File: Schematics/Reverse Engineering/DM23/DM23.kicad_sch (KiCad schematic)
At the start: 100 parts, among them J1 Conn_01x40, Q1 2N1499A, Q2 2N1499A, Q3 2N1499A, Q4 2N1499A, Q5 2N1499A, Q6 2N1499A, Q7 2N1499A, Q8 2N1499A, Q9 2N1499A

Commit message: Updated Schematic Layout and PCB
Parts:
- R39: footprint (none) -> Resistor_THT:R_Axial_DIN0207_L6.3mm_D2.5mm_P10.16mm_Horizontal
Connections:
- net P11 is gone; now on net J1-11: C20.1
- net P13 is gone; now on net J1-13: D12.2 (A)
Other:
- note added: "C4, C12, C19 - Nytronics Type 105 Polyester Film Cap All Diodes are Germanium All Transistor are 2N1499A All Resistors are 1/2W 5% Carbon Composition"
- note added: "| IN | OUT | | 0V | -12V | |-12V| 0V |"
- note removed: "C4, C12, C19 - Nytronics Type 105 Polyester Filt Cap All Diodes are Germanium All Transistor are 2N1499A All Resistors are 1/2W 5% Carbon Composition"
- note removed: "Check Black Resistor for actual value and tolerance"
- moved on the sheet: C1, C10, C11, C12, C13, C14, C15, C16, C17, C18, C19, C2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

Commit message: LR312 Schematic and PCB
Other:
- note added: "C4, C12, C19 - Nytronics Type 105 Polyester Film Cap All Diodes are Germanium All Transistor are 2N1499A All Resistors are 1/2W 5% Carbon Composition Connector Elco Varicon 7000 or 5203 Series Contacts"
- note removed: "C4, C12, C19 - Nytronics Type 105 Polyester Film Cap All Diodes are Germanium All Transistor are 2N1499A All Resistors are 1/2W 5% Carbon Composition"
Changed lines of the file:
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@@
 		)
 	)
-	(text "C4, C12, C19 - Nytronics Type 105 Polyester Film Cap\nAll Diodes are Germanium\nAll Transistor are 2N1499A\nAll Resistors are 1/2W 5% Carbon Composition "
+	(text "C4, C12, C19 - Nytronics Type 105 Polyester Film Cap\nAll Diodes are Germanium\nAll Transistor are 2N1499A\nAll Resistors are 1/2W 5% Carbon Composition \nConnector Elco Varicon 7000 or 5203 Series Contacts"
 		(exclude_from_sim no)
 		(at 211.836 173.736 0)

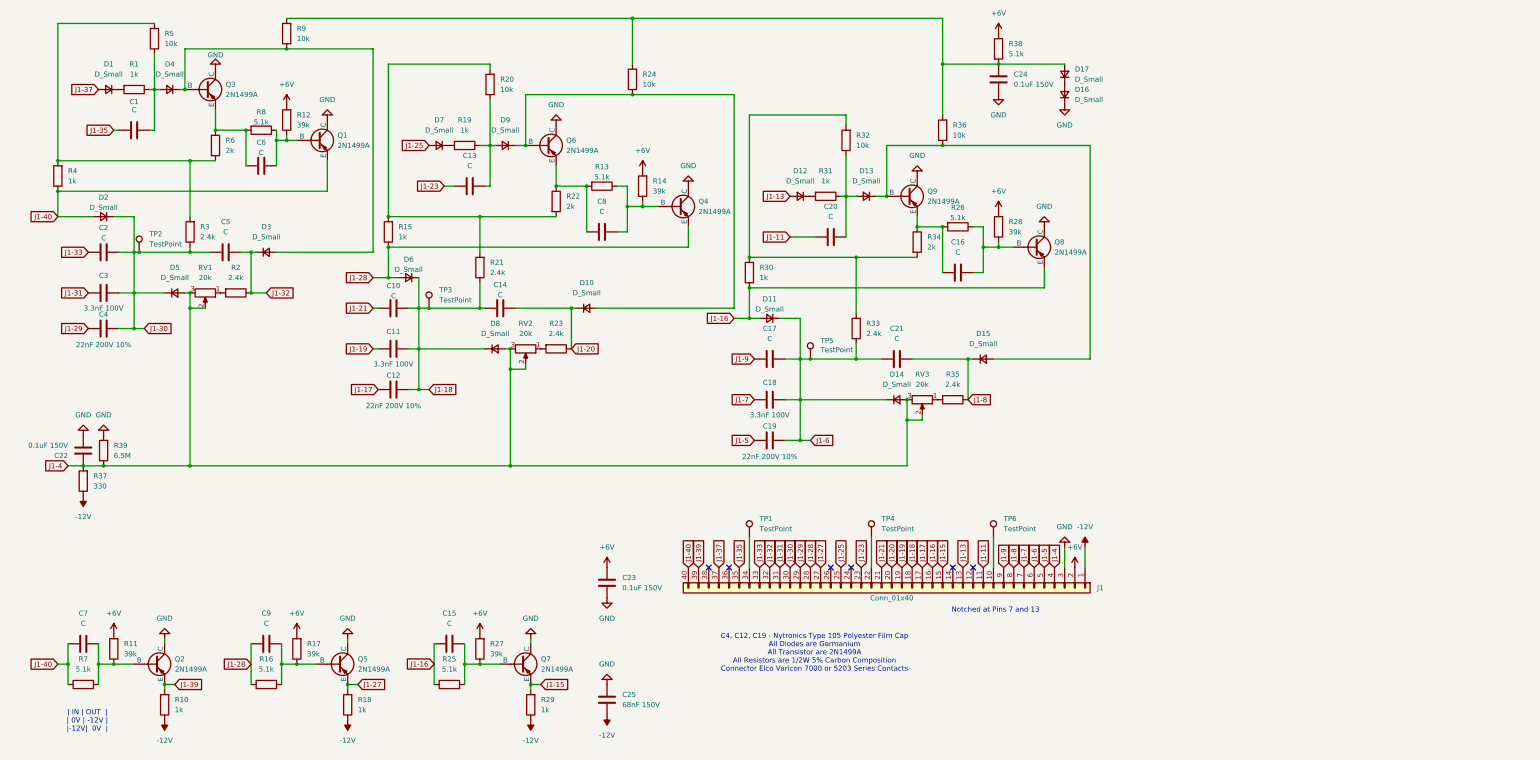
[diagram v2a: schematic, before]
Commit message: DM23 Reverse Engineering Complete
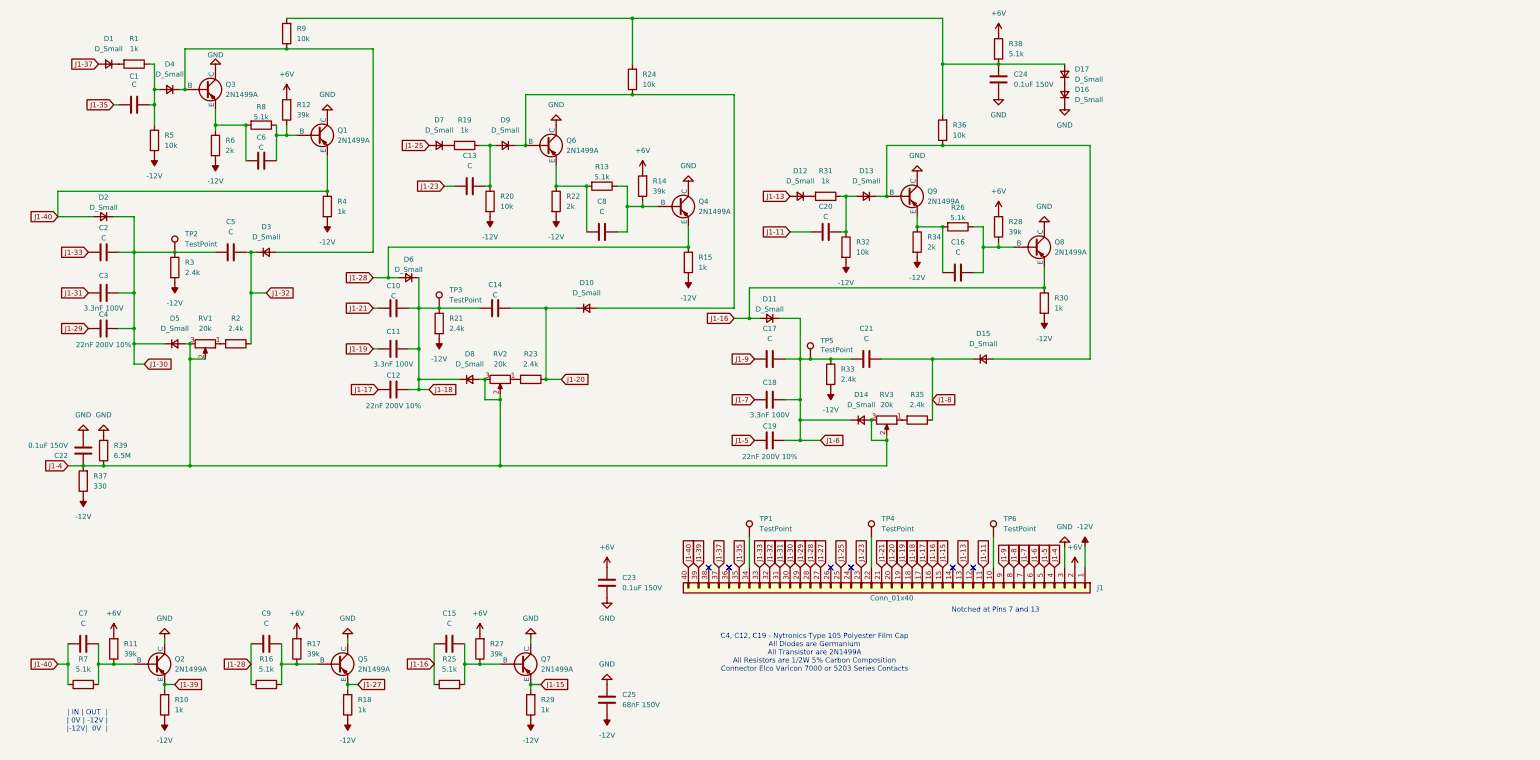
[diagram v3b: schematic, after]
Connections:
- net -12V: now also R15.2, R20.2, R21.2, R22.2, R3.2, R30.2, R32.2, R33.2, R34.2, R4.2, R5.2, R6.2
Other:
- moved on the sheet: C1, C14, C20, C21, C5, C6, D1, D14, D5, D8, Q1, R1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

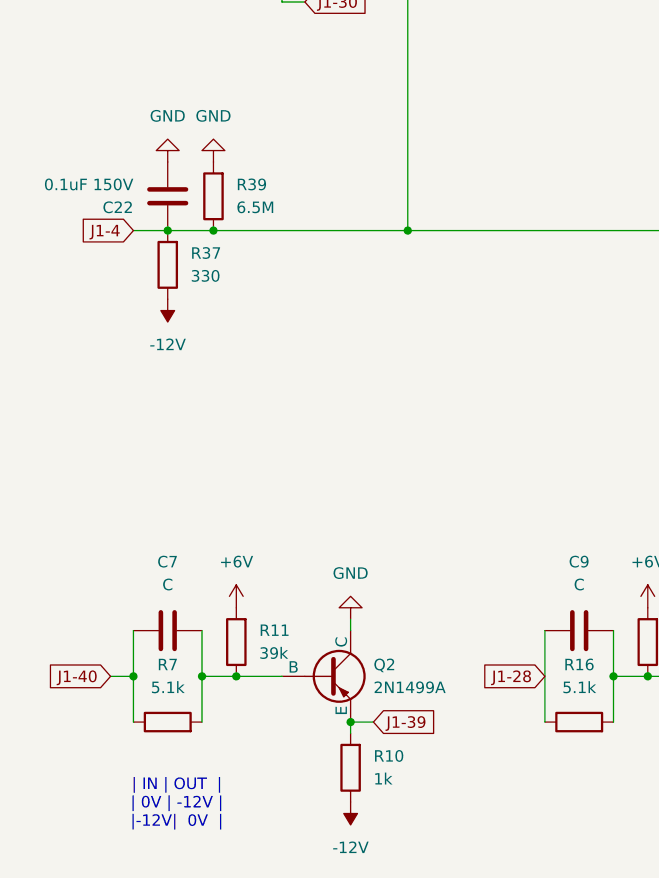
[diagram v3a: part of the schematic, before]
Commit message: Fixed Missing Zener in DM23 and Added MS01 pdf
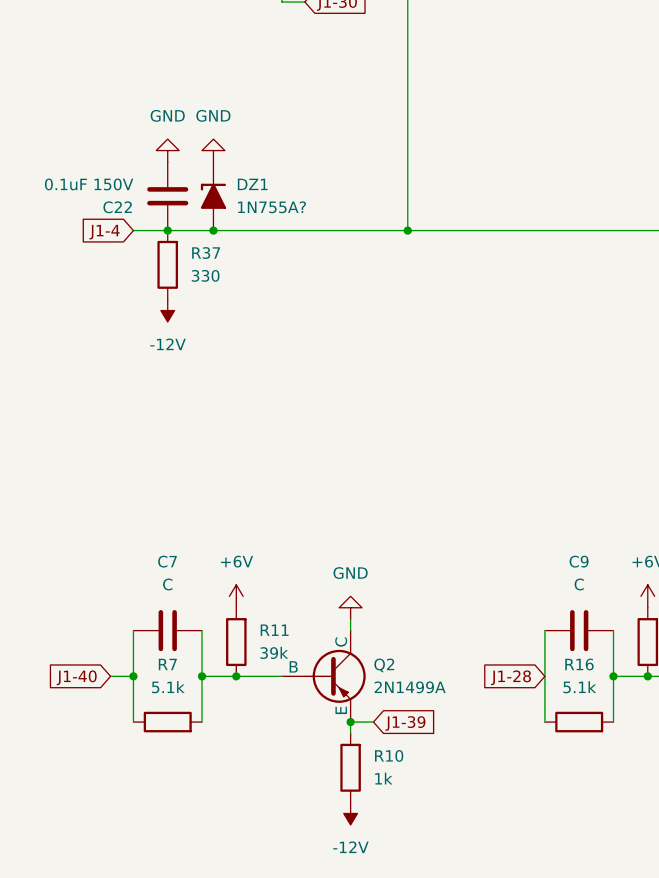
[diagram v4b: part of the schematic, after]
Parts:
- removed R39: 6.5M, Resistor_THT:R_Axial_DIN0207_L6.3mm_D2.5mm_P10.16mm_Horizontal, symbol Device:R
- added DZ1: 1N755A?, Diode_THT:D_A-405_P12.70mm_Horizontal, symbol PCM_Diode_Zener_AKL:D_Zener_Generic
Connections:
- net GND: now also DZ1.1 (K)
- net J1-4: now also DZ1.2 (A)
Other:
- note removed: "| IN | OUT | | 0V | -12V | |-12V| 0V |"
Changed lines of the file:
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@@
 		)
 	)
-	(text "| IN | OUT  |\n| 0V | -12V |\n|-12V|  0V  |"
-		(exclude_from_sim no)
-		(at 30.226 190.754 0)
-		(effects
-			(font
-				(size 1.27 1.27)
-			)
-		)
-	)
 	(text "C4, C12, C19 - Nytronics Type 105 Polyester Film Cap\nAll Diodes are Germanium\nAll Transistor are 2N1499A\nAll Resistors are 1/2W 5% Carbon Composition \nConnector Elco Varicon 7000 or 5203 Series Contacts"
 		(exclude_from_sim no)
@@
 	)
 	(junction
+		(at 34.29 127)
+		(diameter 0)
+		(color 0 0 0 0)
+	)
+	(junction
 		(at 71.12 83.82)
 		(diameter 0)
@@
 	)
 	(junction
-		(at 34.29 127)
-		(diameter 0)
-		(color 0 0 0 0)
-	)
-	(junction
 		(at 29.21 127)
 		(diameter 0)
@@
 	(wire
 		(pts
+			(xy 34.29 127) (xy 55.88 127)
+		)
+		(stroke
+			(width 0)
+			(type default)
+		)
+	)
+	(wire
+		(pts
 			(xy 274.32 147.32) (xy 274.32 152.4)
 		)
@@
 	(wire
 		(pts
-			(xy 55.88 127) (xy 34.29 127)
-		)
-		(stroke
-			(width 0)
-			(type default)
-		)
-	)
-	(wire
-		(pts
 			(xy 118.11 87.63) (xy 128.27 87.63)
 		)
@@
 	)
 	(symbol
+		(lib_id "PCM_Diode_Zener_AKL:D_Zener_Generic")
+		(at 34.29 123.19 90)
+		(unit 1)
+		(exclude_from_sim no)
+		(in_bom yes)
+		(on_board yes)
+		(dnp no)
+		(fields_autoplaced yes)
+		(property "Reference" "DZ1"
+			(at 36.83 121.9199 90)
+			(effects
+				(font
+					(size 1.27 1.27)
+				)
+				(justify right)
+			)
+		)
+		(property "Value" "1N755A?"
+			(at 36.83 124.4599 90)
+			(effects
+				(font
+					(size 1.27 1.27)
+				)
+				(justify right)
+			)
+		)
+		(property "Footprint" "Diode_THT:D_A-405_P12.70mm_Horizontal"
+			(at 34.29 123.19 0)
+			(effects
+				(font
+					(size 1.27 1.27)
+				)
+				(hide yes)
+			)
+		)
+		(property "Datasheet" "~"
+			(at 34.29 123.19 0)
+			(effects
+				(font
+					(size 1.27 1.27)
+				)
+				(hide yes)
+			)
+		)
+		(property "Description" "Zener diode, generic symbol, Alternate KiCAD Library"
+			(at 34.29 123.19 0)
+			(effects
+				(font
+					(size 1.27 1.27)
+				)
+				(hide yes)
+			)
+		)
+		(pin "2"
+		)
+		(pin "1"
+		)
+		(instances
+			(project ""
+				(path "/c123ad63-9ec8-4333-bd1b-94003c898417"
+					(reference "DZ1")
+					(unit 1)
+				)
+			)
+		)
+	)
+	(symbol
 		(lib_id "Device:R")
 		(at 62.23 46.99 0)
@@
 					(unit 1)
 				)
-			)
-		)
-	)
-	(symbol
-		(lib_id "Device:R")
-		(at 34.29 123.19 180)
-		(unit 1)
-		(exclude_from_sim no)
-		(in_bom yes)
-		(on_board yes)
-		(dnp no)
-		(fields_autoplaced yes)
-		(property "Reference" "R39"
-			(at 36.83 121.9199 0)
-			(effects
-				(font
-					(size 1.27 1.27)
-				)
-				(justify right)
-			)
-		)
-		(property "Value" "6.5M"
-			(at 36.83 124.4599 0)
-			(effects
-				(font
-					(size 1.27 1.27)
-				)
-				(justify right)
-			)
-		)
-		(property "Footprint" "Resistor_THT:R_Axial_DIN0207_L6.3mm_D2.5mm_P10.16mm_Horizontal"
-			(at 36.068 123.19 90)
-			(effects
-				(font
-					(size 1.27 1.27)
-				)
-				(hide yes)
-			)
-		)
-		(property "Datasheet" "~"
-			(at 34.29 123.19 0)
-			(effects
-				(font
-					(size 1.27 1.27)
-				)
-				(hide yes)
-			)
-		)
-		(property "Description" "Resistor"
-			(at 34.29 123.19 0)
-			(effects
-				(font
-					(size 1.27 1.27)
-				)
-				(hide yes)
-			)
-		)
-		(pin "1"
-		)
-		(pin "2"
-		)
-		(instances
-			(project ""
-				(path "/c123ad63-9ec8-4333-bd1b-94003c898417"
-					(reference "R39")
-					(unit 1)
-				)
